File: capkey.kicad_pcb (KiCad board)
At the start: 2 copper layers, 44 x 29 mm, 19 parts, among them J1 TIP, J2 RING, J3 AudioJack4, Q1 Q_NMOS_DGS, Q2 Q_NMOS_DGS, SW1 SW_SPDT, U1 AT42QT1011-TSHR, U2 AT42QT1011-TSHR, U3 L78L05_SOT89

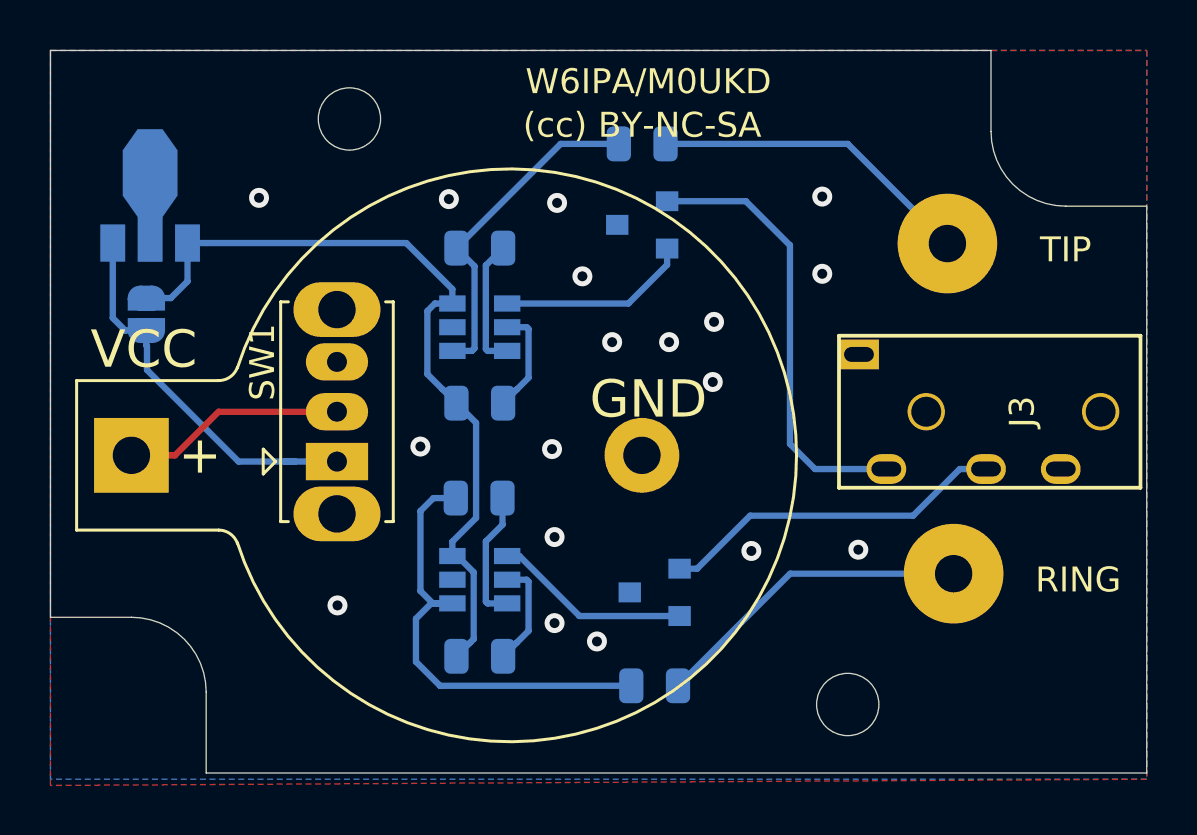
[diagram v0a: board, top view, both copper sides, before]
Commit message: switched paddle sides
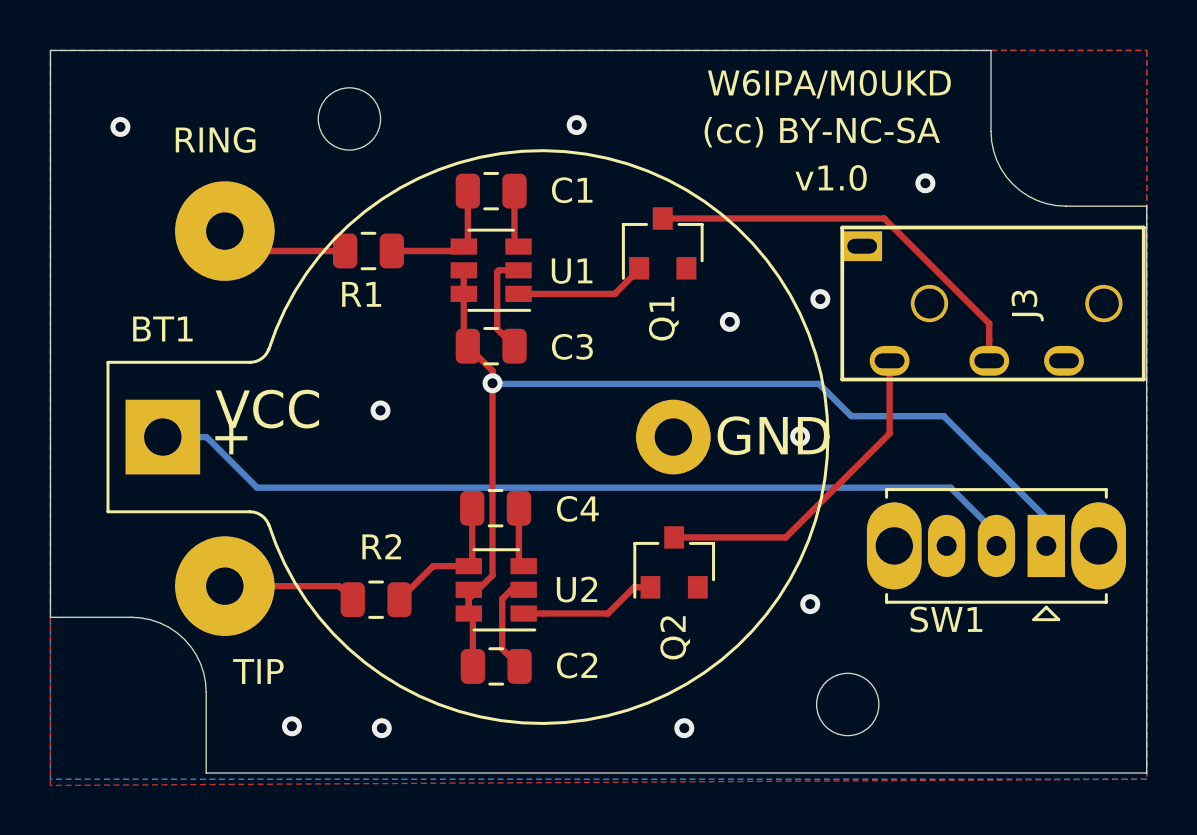
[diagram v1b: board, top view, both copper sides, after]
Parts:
- removed JP1: SolderJumper_2_Open, Jumper:SolderJumper-2_P1.3mm_Open_RoundedPad1.0x1.5mm
- removed U3: L78L05_SOT89, Package_TO_SOT_SMD:SOT-89-3
- added LOGO1: dahu-logo, w6ipa-footprints:W6IPA-Logo-9mmx8mm, B.Cu at (157.5, 44.3)
- C1, C2, C3, C4, R1, R2, U1, U2: moved to F.Cu
- Q1, Q2: value Q_NMOS_DGS -> IRFML8244TRPbF; moved to F.Cu
- moved J2 29.3 mm to (146.0, 51.5)
- moved J1 29.0 mm to (146.0, 37.2), turned to 90 degrees
- moved SW1 28.7 mm to (179.0, 49.9), turned to 180 degrees
- moved R1 11.8 mm to (151.8, 38.0), turned to 180 degrees
- moved R2 11.7 mm to (152.1, 52.0), turned to 180 degrees
- moved J3 4.34 mm to (182.9, 40.2)
- moved C1 2.33 mm to (156.7, 35.6)
- moved C3 2.33 mm to (156.7, 41.9)
- moved U1 2.33 mm to (156.7, 38.8)
- moved BT1 1.46 mm to (143.5, 45.5)
- moved Q2 1.44 mm to (164.0, 50.5), turned to 90 degrees
- moved Q1 1.11 mm to (163.6, 37.7), turned to 90 degrees
- moved C4 0.78 mm to (156.9, 48.4)
- moved C2 0.78 mm to (156.9, 54.7)
- moved U2 0.78 mm to (156.9, 51.6)
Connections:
- Q1 pad 1: tip -> Net-(Q1-Pad1)
- Q1 pad 2: Net-(Q1-Pad2) -> sleeve
- Q1 pad 3: sleeve -> ring
- Q2 pad 1: ring -> Net-(Q2-Pad1)
- Q2 pad 2: Net-(Q2-Pad2) -> sleeve
- Q2 pad 3: sleeve -> tip
- SW1 pad 1: Net-(JP1-Pad1) -> Net-(C2-Pad1)
- U1 pad 1: Net-(Q1-Pad2) -> Net-(Q1-Pad1)
- U2 pad 1: Net-(Q2-Pad2) -> Net-(Q2-Pad1)
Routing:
- net +3V0: track 8.97 -> 35.6 mm
- net Net-(JP1-Pad1): track 15.7 -> 0.00 mm
- net Net-(C4-Pad2): track 18.8 -> 5.73 mm
- net Net-(C2-Pad1): track 32.4 -> 43.9 mm, vias 0 -> 1
- net Net-(C1-Pad2): track 13.5 -> 5.25 mm
- net Net-(Q2-Pad2): track 7.92 -> 0.00 mm
- net Net-(J1-Pad1): track 13.0 -> 5.16 mm
- net Net-(Q1-Pad2): track 7.72 -> 0.00 mm
- net Net-(J2-Pad1): track 12.9 -> 5.36 mm
- net Net-(Q2-Pad1): track 0.00 -> 5.53 mm
- net Net-(Q1-Pad1): track 0.00 -> 5.29 mm
- net tip: track 17.9 -> 13.3 mm
- net Net-(C1-Pad1): track 5.23 -> 2.29 mm
- net Net-(C4-Pad1): track 5.32 -> 2.40 mm
- net ring: track 14.0 -> 16.3 mm
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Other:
- board text added: "v1.0"

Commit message: v1.0
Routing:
- net sleeve: track 8.16 -> 5.42 mm, vias 11 -> 13
- net Net-(C2-Pad1): track 43.9 -> 45.0 mm
